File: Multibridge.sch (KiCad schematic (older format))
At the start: 2 parts

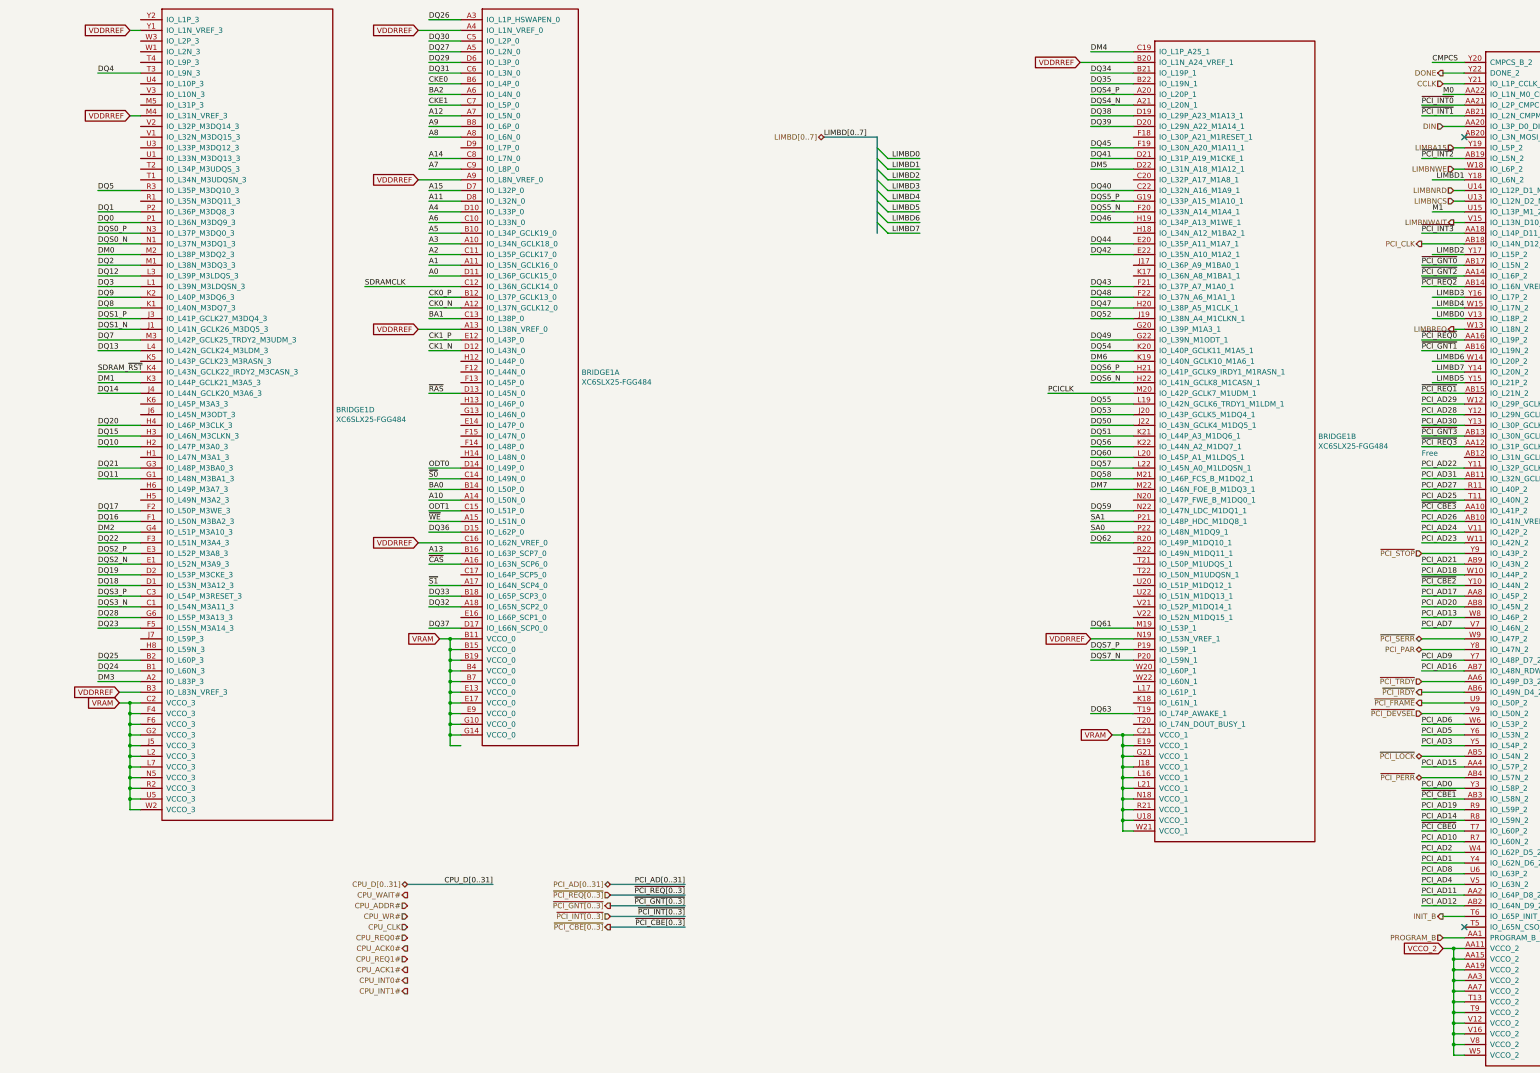
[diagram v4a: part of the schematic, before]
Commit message: Route CPU bus and cache
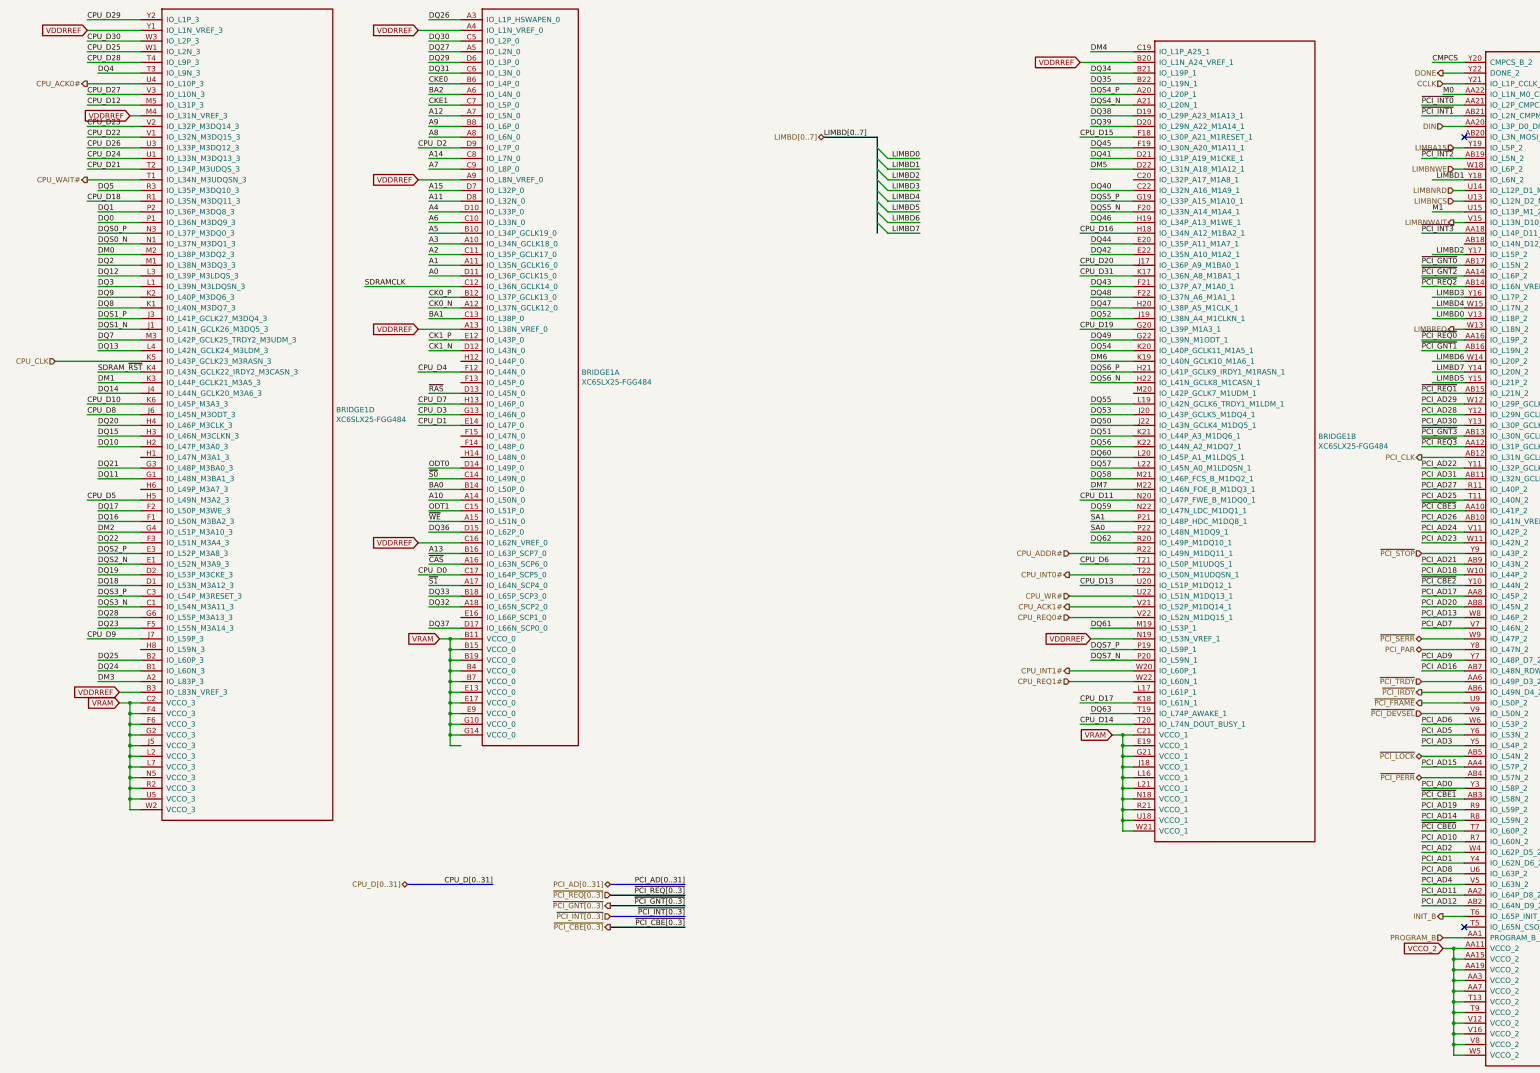
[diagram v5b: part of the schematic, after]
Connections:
- net labels added: CPU_D0, CPU_D1, CPU_D10, CPU_D11, CPU_D12, CPU_D13, CPU_D14, CPU_D15, CPU_D16, CPU_D17, CPU_D18, CPU_D19, CPU_D2, CPU_D20, CPU_D21, CPU_D22, CPU_D23, CPU_D24, CPU_D25, CPU_D26, CPU_D27, CPU_D28, CPU_D29, CPU_D3, CPU_D30, CPU_D31, CPU_D4, CPU_D5, CPU_D6, CPU_D7, CPU_D8, CPU_D9
- net labels removed: PCICLK
- wire segments 393 -> 434
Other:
- note removed: "Free"
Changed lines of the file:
@@
 Text GLabel 1800 2200 0    50   Input ~ 0
 VDDRREF
-Text GLabel 1800 1400 0    50   Input ~ 0
+Text GLabel 1400 1400 0    50   Input ~ 0
 VDDRREF
 $Comp
@@
 Text Label 4000 3800 0    50   ~ 0
 SDRAMCLK
-Text Label 10400 4800 0    50   ~ 0
-PCICLK
 Text HLabel 4400 9400 0    50   BiDi ~ 0
 CPU_D[0..31]
 Text Label 5200 9400 2    50   ~ 0
 CPU_D[0..31]
-Text HLabel 4400 9500 0    50   Output ~ 0
+Text HLabel 1400 2800 0    50   Output ~ 0
 CPU_WAIT#
-Text HLabel 4400 9600 0    50   Input ~ 0
+Text HLabel 10600 6300 0    50   Input ~ 0
 CPU_ADDR#
-Text HLabel 4400 9700 0    50   Input ~ 0
+Text HLabel 10600 6700 0    50   Input ~ 0
 CPU_WR#
-Text HLabel 4400 9800 0    50   Input ~ 0
+Text HLabel 1100 4500 0    50   Input ~ 0
 CPU_CLK
-Text HLabel 4400 9900 0    50   Input ~ 0
+Text HLabel 10600 6900 0    50   Input ~ 0
 CPU_REQ0#
-Text HLabel 4400 10000 0    50   Output ~ 0
+Text HLabel 1400 1900 0    50   Output ~ 0
 CPU_ACK0#
-Text HLabel 4400 10100 0    50   Input ~ 0
+Text HLabel 10600 7500 0    50   Input ~ 0
 CPU_REQ1#
-Text HLabel 4400 10200 0    50   Output ~ 0
+Text HLabel 10600 6800 0    50   Output ~ 0
 CPU_ACK1#
-Text HLabel 4400 10300 0    50   Output ~ 0
+Text HLabel 10600 6500 0    50   Output ~ 0
 CPU_INT0#
-Text HLabel 4400 10400 0    50   Output ~ 0
+Text HLabel 10600 7400 0    50   Output ~ 0
 CPU_INT1#
 Text HLabel 6300 9400 0    50   BiDi ~ 0
@@
 Text Label 13900 3300 0    50   ~ 0
 ~PCI_INT3
-Text HLabel 13900 3400 0    50   Output ~ 0
+Text HLabel 13900 5400 0    50   Output ~ 0
 PCI_CLK
 Text HLabel 6300 9800 0    50   Output ~ 0
@@
 	1800 2200 1900 2200
 Wire Wire Line
-	1800 1400 1900 1400
+	1400 1400 1900 1400
 Wire Wire Line
 	4500 1400 4900 1400
@@
 	14200 4200 14300 4200
 Wire Wire Line
-	13900 3400 14300 3400
+	13900 5400 14300 5400
 Wire Wire Line
 	13900 3600 14300 3600
@@
 Wire Wire Line
 	4900 3800 4000 3800
-Wire Wire Line
-	10400 4800 11200 4800
 Wire Bus Line
 	4400 9400 5200 9400
@@
 Text HLabel 13900 7200 0    50   BiDi ~ 0
 PCI_PAR
-Text Notes 13900 5400 0    50   ~ 0
-Free
+Wire Wire Line
+	1100 4500 1900 4500
+Text Label 4500 6500 0    50   ~ 0
+CPU_D0
+Wire Wire Line
+	4500 6500 4900 6500
+Text Label 4500 5100 0    50   ~ 0
+CPU_D1
+Wire Wire Line
+	4900 5100 4500 5100
+Text Label 4500 2500 0    50   ~ 0
+CPU_D2
+Wire Wire Line
+	4500 2500 4900 2500
+Text Label 4500 5000 0    50   ~ 0
+CPU_D3
+Wire Wire Line
+	4500 5000 4900 5000
+Text Label 4500 4600 0    50   ~ 0
+CPU_D4
+Wire Wire Line
+	4500 4600 4900 4600
+Text Label 1400 5800 0    50   ~ 0
+CPU_D5
+Wire Wire Line
+	1400 5800 1900 5800
+Text Label 4500 4900 0    50   ~ 0
+CPU_D7
+Wire Wire Line
+	4500 4900 4900 4900
+Text Label 1400 5000 0    50   ~ 0
+CPU_D8
+Wire Wire Line
+	1400 5000 1900 5000
+Text Label 1400 7100 0    50   ~ 0
+CPU_D9
+Wire Wire Line
+	1400 7100 1900 7100
+Text Label 1400 4900 0    50   ~ 0
+CPU_D10
+Wire Wire Line
+	1400 4900 1900 4900
+Text Label 10700 5800 0    50   ~ 0
+CPU_D11
+Wire Wire Line
+	10700 5800 11200 5800
+Text Label 1400 2100 0    50   ~ 0
+CPU_D12
+Wire Wire Line
+	1400 2100 1900 2100
+Text Label 10700 6600 0    50   ~ 0
+CPU_D13
+Wire Wire Line
+	10700 6600 11200 6600
+Text Label 10700 7900 0    50   ~ 0
+CPU_D14
+Wire Wire Line
+	10700 7900 11200 7900
+Text Label 10700 2400 0    50   ~ 0
+CPU_D15
+Wire Wire Line
+	10700 2400 11200 2400
+Text Label 10700 3300 0    50   ~ 0
+CPU_D16
+Wire Wire Line
+	10700 3300 11200 3300
+Text Label 10700 7700 0    50   ~ 0
+CPU_D17
+Wire Wire Line
+	10700 7700 11200 7700
+Text Label 10700 6400 0    50   ~ 0
+CPU_D6
+Wire Wire Line
+	10700 6400 11200 6400
+Text Label 1400 3000 0    50   ~ 0
+CPU_D18
+Wire Wire Line
+	1400 3000 1900 3000
+Text Label 10700 4200 0    50   ~ 0
+CPU_D19
+Wire Wire Line
+	10700 4200 11200 4200
+Text Label 10700 3600 0    50   ~ 0
+CPU_D20
+Wire Wire Line
+	10700 3600 11200 3600
+Text Label 10700 3700 0    50   ~ 0
+CPU_D31
+Wire Wire Line
+	10700 3700 11200 3700
+Text Label 1400 2700 0    50   ~ 0
+CPU_D21
+Wire Wire Line
+	1400 2700 1900 2700
+Text Label 1400 2400 0    50   ~ 0
+CPU_D22
+Wire Wire Line
+	1400 2400 1900 2400
+Wire Wire Line
+	1400 2800 1900 2800
+Text Label 1400 2600 0    50   ~ 0
+CPU_D24
+Wire Wire Line
+	1400 2600 1900 2600
+Text Label 1400 1600 0    50   ~ 0
+CPU_D25
+Wire Wire Line
+	1400 1600 1900 1600
+Text Label 1400 2300 0    50   ~ 0
+CPU_D23
+Wire Wire Line
+	1400 2300 1900 2300
+Text Label 1400 1700 0    50   ~ 0
+CPU_D28
+Wire Wire Line
+	1400 1700 1900 1700
+Text Label 1400 1300 0    50   ~ 0
+CPU_D29
+Wire Wire Line
+	1400 1300 1900 1300
+Text Label 1400 2500 0    50   ~ 0
+CPU_D26
+Wire Wire Line
+	1400 2500 1900 2500
+Text Label 1400 2000 0    50   ~ 0
+CPU_D27
+Wire Wire Line
+	1400 2000 1900 2000
+Wire Wire Line
+	1400 1900 1900 1900
+Text Label 1400 1500 0    50   ~ 0
+CPU_D30
+Wire Wire Line
+	1400 1500 1900 1500
+Wire Wire Line
+	11200 6300 10600 6300
+Wire Wire Line
+	10600 6700 11200 6700
+Wire Wire Line
+	10600 6500 11200 6500
+Wire Wire Line
+	10600 6900 11200 6900
+Wire Wire Line
+	10600 6800 11200 6800
+Wire Wire Line
+	10600 7400 11200 7400
+Wire Wire Line
+	10600 7500 11200 7500
 $EndSCHEMATC

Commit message: power, yo
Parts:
- added C100, C101, C102, C103, C104, C105, C106, C107, C108, C109, C98, C99: 1u, IPC7351-Nominal:CAPC1005X55, symbol C-0402
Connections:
- net labels added: GND, P1V5_BRIDGE, P3V3_BRIDGE
- net labels removed: VCCO_2, VRAM
- wire segments 434 -> 466

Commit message: TODO: learn to write good commit messages
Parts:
- added C115: 1u, IPC7351-Nominal:CAPC1005X55, symbol C-0402
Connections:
- net labels added: P3V3_STBY
- wire segments 466 -> 468
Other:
- note added: "Ground current bypass for EC bus"
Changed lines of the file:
@@
 LIBS:semi-diode-Panasonic
 LIBS:Murata
+LIBS:semi-trans-Panasonic
 LIBS:c4puter-cache
 EELAYER 25 0
@@
 P 3600 10600
 AR Path="/5763AB3B/5799D8FC" Ref="#PWR?"  Part="1"
-AR Path="/5763A638/5799D8FC" Ref="#PWR146"  Part="1"
-F 0 "#PWR146" H 3600 10600 30  0001 C CNN
+AR Path="/5763A638/5799D8FC" Ref="#PWR162"  Part="1"
+F 0 "#PWR162" H 3600 10600 30  0001 C CNN
 F 1 "GND" H 3600 10530 30  0001 C CNN
 F 2 "" H 3600 10600 60  0000 C CNN
@@
 P3V3_BRIDGE
 $Comp
-L GND #PWR147
+L GND #PWR163
 U 1 1 5799E8A3
 P 12900 10600
-F 0 "#PWR147" H 12900 10600 30  0001 C CNN
+F 0 "#PWR163" H 12900 10600 30  0001 C CNN
 F 1 "GND" H 12900 10530 30  0001 C CNN
 F 2 "" H 12900 10600 60  0000 C CNN
@@
 Wire Wire Line
 	11700 10500 12900 10500
+$Comp
+L C-0402 C?
+U 1 1 579C48FF
+P 12200 11100
+AR Path="/5765A5BA/579C48FF" Ref="C?"  Part="1"
+AR Path="/5765B2E6/579C48FF" Ref="C?"  Part="1"
+AR Path="/5763AB3B/579C48FF" Ref="C?"  Part="1"
+AR Path="/5763A638/579C48FF" Ref="C115"  Part="1"
+F 0 "C115" V 11950 11100 50  0000 C CNN
+F 1 "1u" V 12041 11100 50  0000 C CNN
+F 2 "IPC7351-Nominal:CAPC1005X55" H 12200 11100 50  0001 C CNN
+F 3 "http://psearch.en.murata.com/capacitor/product/GRM155C80J105KE15%23.html" H 12190 11075 60  0001 C CNN
+F 4 "DIST DIGIKEY 490-6281-1-ND" H 13000 11650 60  0001 C CNN "BOM"
+	1    12200 11100
+	0    1    1    0
+$EndComp
+Text GLabel 12400 11100 2    50   Input ~ 0
+P3V3_BRIDGE
+Wire Wire Line
+	12400 11100 12300 11100
+Text GLabel 12000 11100 0    50   Input ~ 0
+P3V3_STBY
+Wire Wire Line
+	12000 11100 12100 11100
+Text Notes 11650 11300 0    50   ~ 0
+Ground current bypass for EC bus
 $EndSCHEMATC
